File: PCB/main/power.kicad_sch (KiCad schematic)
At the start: 19 parts

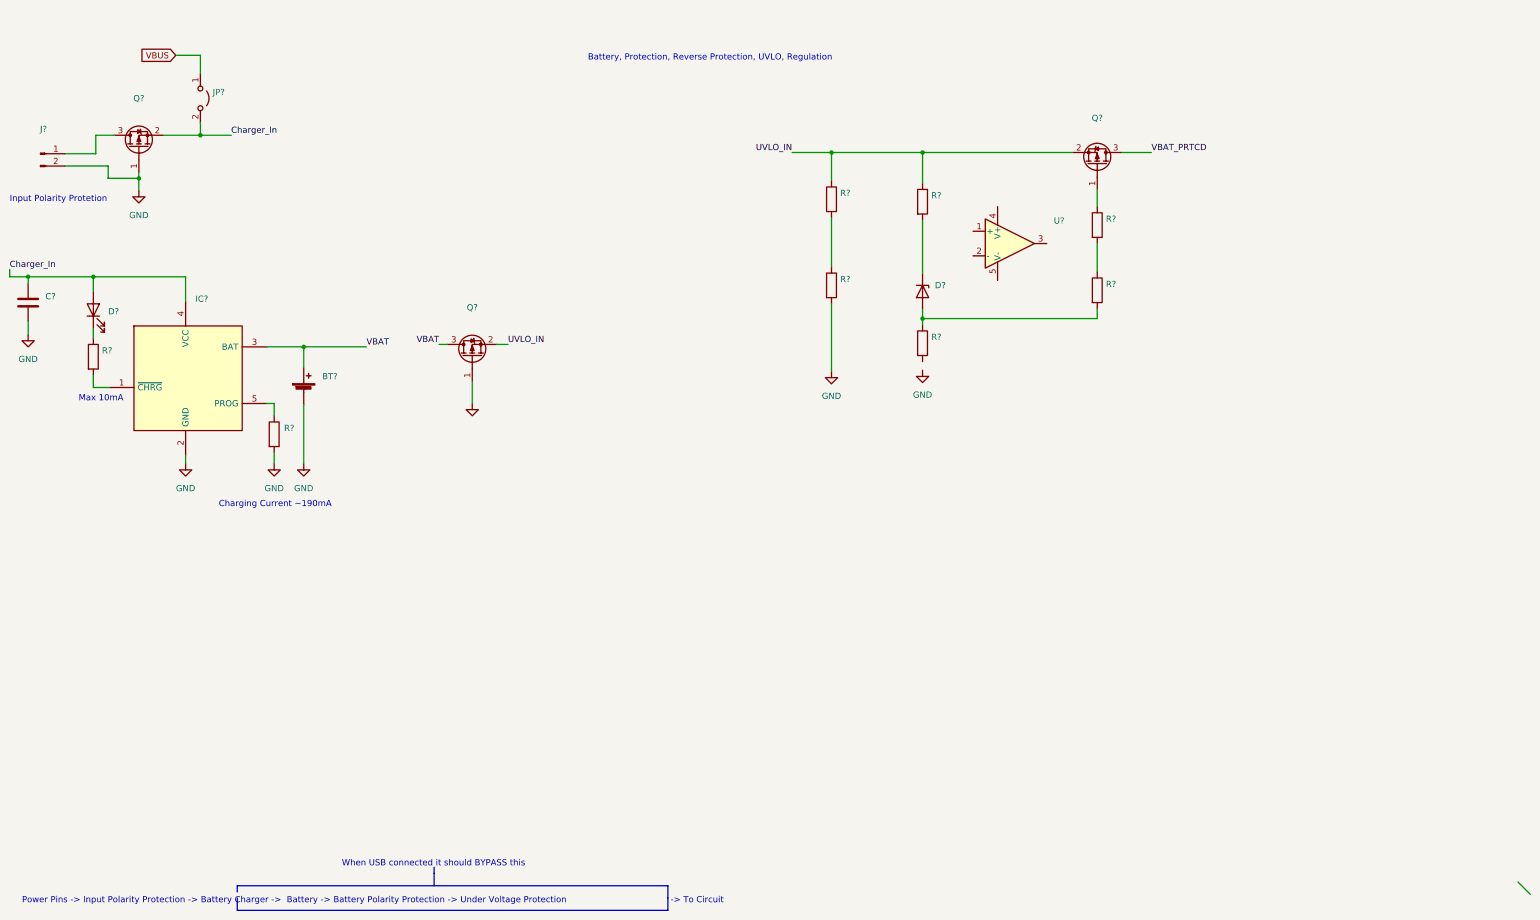
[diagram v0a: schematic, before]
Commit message: updated UVLO circuit
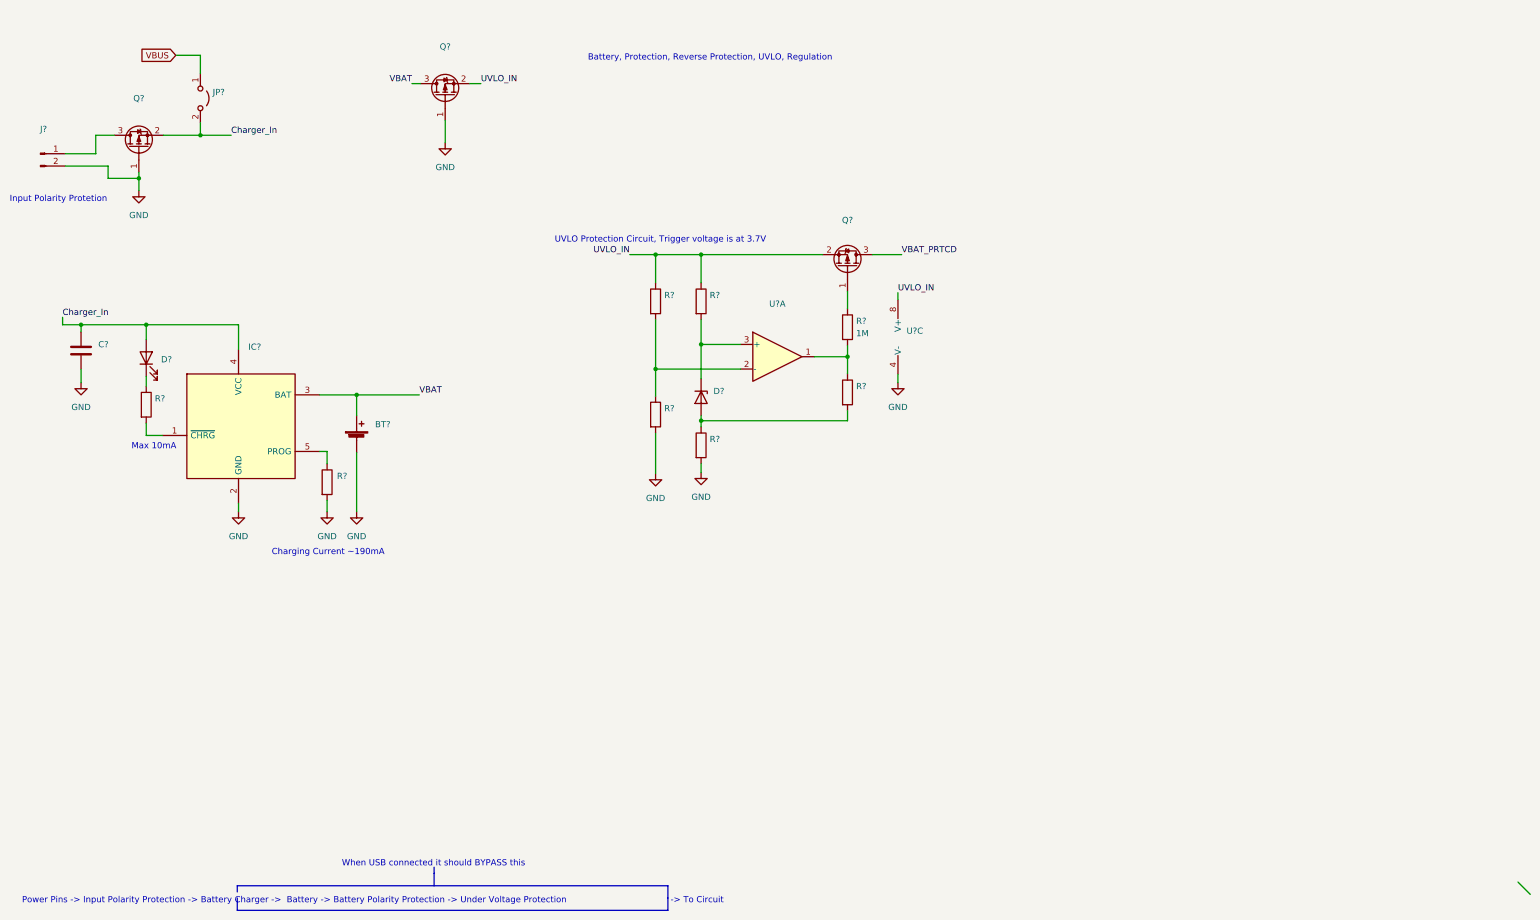
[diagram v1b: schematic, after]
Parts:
- removed R?: (no value), symbol Device:R
- removed U?: (no value), symbol pspice:OPAMP
- added R?: 1M, Resistor_SMD:R_0603_1608Metric_Pad0.98x0.95mm_HandSolder, symbol Device:R
- added U? (x2): (no value), symbol Amplifier_Operational:LM358
- R?: Populate (none) -> Y; Price (none) -> 0.0013
- R?: Populate (none) -> Y; Price (none) -> 0.0014
- R?: LCSC (none) -> C8218; Price (none) -> 0.0013
- R?: LCSC (none) -> C22775; Populate (none) -> Y; Price (none) -> 0.0013
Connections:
- net GND: now also R?.2, U?.4 (V-)
- net UVLO_IN: now also U?.8 (V+)
- net at Q?.1 (G): now also R?.1
- net at R?.1, R?.2: now also U?.2 (-)
- net at D?.1 (K), R?.2: now also U?.3 (+)
- net at R?.1: now also R?.2, U?.1
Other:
- note added: "UVLO Protection Circuit, Trigger voltage is at 3.7V"
- moved on the sheet: BT?, C?, D?, IC?, Q?, R?

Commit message: added digital sensors
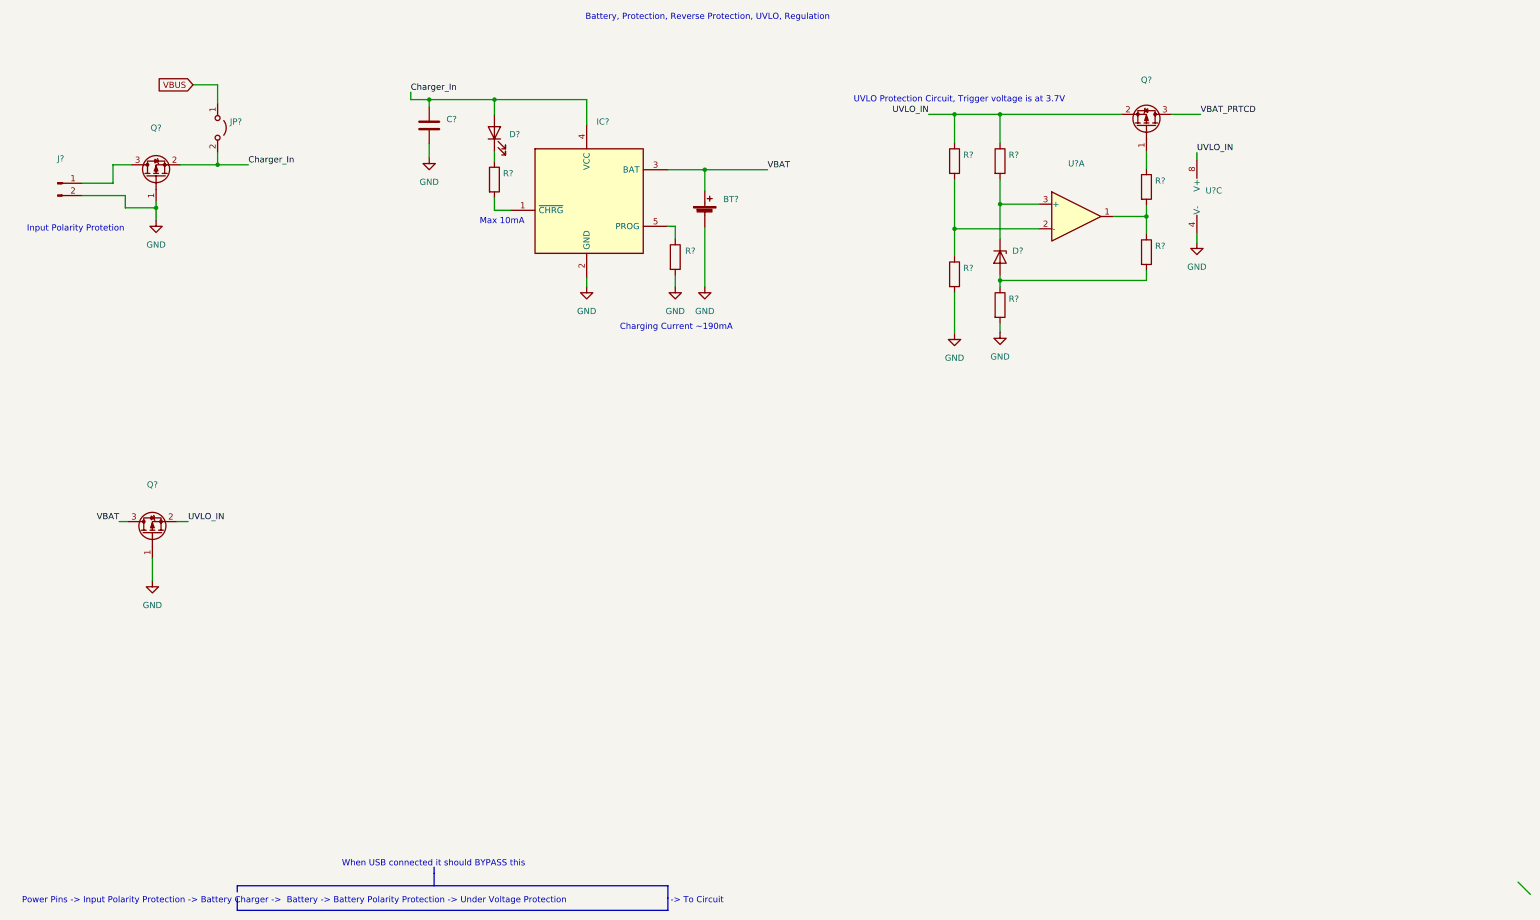
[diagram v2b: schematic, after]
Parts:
- R?: value 1M -> (none); footprint Resistor_SMD:R_0603_1608Metric_Pad0.98x0.95mm_HandSolder -> (none)
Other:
- company: (none) -> University of Cape Town
- title: (none) -> DiscoverAir HAT
- moved on the sheet: BT?, C?, D?, IC?, J?, JP?, Q?, R?, U?A, U?C

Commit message: layout started
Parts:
- removed J?: (no value), symbol Connector:Conn_01x02_Male
- removed JP?: (no value), symbol Jumper:Jumper_2_Open
- added C11, C5, C6, C8, C9: 1uF, Capacitor_SMD:C_0603_1608Metric_Pad1.08x0.95mm_HandSolder, symbol Device:C
- added C7: 10nF, Capacitor_SMD:C_0603_1608Metric_Pad1.08x0.95mm_HandSolder, symbol Device:C
- added D4: D_Schottky, Diode_SMD:D_SMA, symbol Device:D_Schottky
- added J8: Conn_01x02_Male, Connector_PinHeader_2.54mm:PinHeader_1x02_P2.54mm_Vertical, symbol Connector:Conn_01x02_Male
- added JP1, JP2: Jumper_3_Open, Connector_PinHeader_2.54mm:PinHeader_1x03_P2.54mm_Vertical, symbol Jumper:Jumper_3_Open
- added Q3: Q_PMOS_GSD, Package_TO_SOT_SMD:SOT-23, symbol Device:Q_PMOS_GSD
- added R10: 4k7, Resistor_SMD:R_0603_1608Metric_Pad0.98x0.95mm_HandSolder, symbol Device:R
- added R12: 2.2M, Resistor_SMD:R_0603_1608Metric_Pad0.98x0.95mm_HandSolder, symbol Device:R
- added R13: 1M, Resistor_SMD:R_0603_1608Metric_Pad0.98x0.95mm_HandSolder, symbol Device:R
- added TP2: 1V8, symbol Connector:TestPoint_Alt
- added TP4: UVLO_Out, symbol Connector:TestPoint_Alt
- added TP5: REG_IN, symbol Connector:TestPoint_Alt
- added TP6: VBAT, symbol Connector:TestPoint_Alt
- added TP7: UVLO V+, symbol Connector:TestPoint_Alt
- added TP8: UVLO V-, symbol Connector:TestPoint_Alt
- added U2: SGM2007-3.3XN5/TR, Package_TO_SOT_SMD:SOT-23-5, symbol DiscoverAir:SGM2007-3.3XN5/TR
- added U3: AMS1117-1.8, Package_TO_SOT_SMD:SOT-223-3_TabPin2, symbol Regulator_Linear:AMS1117-1.8
- added unit 2 of U4
- BT1: renamed from BT?; value (none) -> Battery_Cell
- C10: renamed from C?; value (none) -> 1uF; footprint (none) -> Capacitor_SMD:C_0603_1608Metric_Pad1.08x0.95mm_HandSolder; LCSC (none) -> C15849
- D3: renamed from D?; value (none) -> CHRG; footprint (none) -> LED_SMD:LED_0603_1608Metric_Pad1.05x0.95mm_HandSolder; LCSC (none) -> C2286
- D5: renamed from D?; value (none) -> D_Zener; footprint (none) -> Diode_SMD:D_SOD-523
- IC3: renamed from IC?; value (none) -> TP4054-42-SOT25-R; footprint (none) -> TP4054-42-SOT25-R:SOT95P280X100-5N; Manufacturer_Name (none) -> TOP POWER
- Q2, Q4, Q5: renamed from Q?; value (none) -> Q_PMOS_GSD; footprint (none) -> Package_TO_SOT_SMD:SOT-23
- R11: renamed from R?; value (none) -> 5K1; footprint (none) -> Resistor_SMD:R_0805_2012Metric_Pad1.20x1.40mm_HandSolder; LCSC (none) -> C23186
- R14: renamed from R?; value (none) -> 300K; footprint (none) -> Resistor_SMD:R_0603_1608Metric_Pad0.98x0.95mm_HandSolder; LCSC C23146 -> C23024; Price 0.0014 -> 0.0013
- R15, R18: renamed from R?; value (none) -> 1M; footprint (none) -> Resistor_SMD:R_0603_1608Metric_Pad0.98x0.95mm_HandSolder
- R16: renamed from R?; value (none) -> 150; footprint (none) -> Resistor_SMD:R_0603_1608Metric_Pad0.98x0.95mm_HandSolder; LCSC C8218 -> C22808; Price 0.0013 -> 0.0016
- R17: renamed from R?; value (none) -> 100; footprint (none) -> Resistor_SMD:R_0603_1608Metric_Pad0.98x0.95mm_HandSolder
- R19: renamed from R?; value (none) -> R; footprint (none) -> Resistor_SMD:R_0603_1608Metric_Pad0.98x0.95mm_HandSolder
- R9: renamed from R?; value (none) -> 510; footprint (none) -> Resistor_SMD:R_0603_1608Metric_Pad0.98x0.95mm_HandSolder; LCSC (none) -> C23193
- U4: renamed from U?; value (none) -> LM358; footprint (none) -> Package_SO:SOIC-8_3.9x4.9mm_P1.27mm; LCSC (none) -> C7950
- U4: renamed from U?; value (none) -> LM358; footprint (none) -> Package_SO:SOIC-8_3.9x4.9mm_P1.27mm
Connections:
- net Charger_In: now also D4.2 (A), J8.1 (Pin_1), Q3.1 (G), R10.2; no longer C10.1, D3.2 (A), IC3.4 (VCC)
- net GND: now also C11.2, C5.2, C6.2, C7.1, C8.2, C9.2, R10.1, R13.2, U2.2 (GND), U3.1 (GND)
- net UVLO_IN: now also R12.1
- net VBAT: now also TP6.1
- net VBAT_PRTCD: now also Q3.3 (D), TP4.1
- net at R14.2, R15.1, U4.2 (-): now also TP7.1
- net at D5.1 (K), R16.2, U4.3 (+): now also TP8.1
- net +5V: now reaches Q2.3 (D)
- net +5V: now also JP1.1 (A), JP2.1 (A)
- new net: C6.1, JP2.2 (C), U3.3 (VI)
- new net: C11.1, R12.2, R13.1, U4.5 (+)
- new net: C10.1, D3.2 (A), IC3.4 (VCC), J8.2 (Pin_2)
- new net: C5.1, JP1.2 (C), U2.1 (IN), U2.3 (EN)
- new net: C7.2, U2.4 (BP)
- new net +1V8: C8.1, TP2.1, U3.2 (VO)
- new net +3V0: C9.1, U2.5 (OUT)
- new net BATTERY_VOLTAGE: U4.6 (-), U4.7
- new net REG_IN: D4.1 (K), JP1.3 (B), JP2.3 (B), Q3.2 (S), TP5.1
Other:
- note added: "1.8V Regulator"
- note added: "3.3V Regulator"
- note added: "Battery Level Sensor"
- note added: "ByPass Battery Switch when USB Powered Allows for battery to charge while circuit is powered by USB"
- note added: "UVLO Protection Circuit, Trigger voltage is at 3.5V"
- note removed: "UVLO Protection Circuit, Trigger voltage is at 3.7V"
- moved on the sheet: Q4

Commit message: started on routing
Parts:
- BT1: footprint (none) -> Battery:BatteryHolder_Keystone_1042_1x18650
- TP2, TP4, TP5, TP6, TP7, TP8: footprint (none) -> TestPoint:TestPoint_Pad_D2.0mm
- U3: value AMS1117-1.8 -> (none); footprint Package_TO_SOT_SMD:SOT-223-3_TabPin2 -> (none)
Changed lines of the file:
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@@
       (effects (font (size 1.27 1.27)) (justify left))
     )
-    (property "Footprint" "" (id 2) (at 132.588 133.096 0)
+    (property "Footprint" "TestPoint:TestPoint_Pad_D2.0mm" (id 2) (at 132.588 133.096 0)
       (effects (font (size 1.27 1.27)) hide)
     )
@@
       (effects (font (size 1.27 1.27)) (justify left))
     )
-    (property "Footprint" "" (id 2) (at 174.244 38.862 0)
+    (property "Footprint" "TestPoint:TestPoint_Pad_D2.0mm" (id 2) (at 174.244 38.862 0)
       (effects (font (size 1.27 1.27)) hide)
     )
@@
     (in_bom yes) (on_board yes) (fields_autoplaced)
     (property "Reference" "U3" (id 0) (at 64.77 134.62 0))
-    (property "Value" "AMS1117-1.8" (id 1) (at 64.77 137.16 0))
-    (property "Footprint" "Package_TO_SOT_SMD:SOT-223-3_TabPin2" (id 2) (at 64.77 136.398 0)
+    (property "Value" "" (id 1) (at 64.77 137.16 0))
+    (property "Footprint" "" (id 2) (at 64.77 136.398 0)
       (effects (font (size 1.27 1.27)) hide)
     )
@@
     (property "Reference" "TP7" (id 0) (at 206.756 43.18 90))
     (property "Value" "UVLO V+" (id 1) (at 208.534 45.974 90))
-    (property "Footprint" "" (id 2) (at 212.852 38.1 0)
+    (property "Footprint" "TestPoint:TestPoint_Pad_D2.0mm" (id 2) (at 212.852 38.1 0)
       (effects (font (size 1.27 1.27)) hide)
     )
@@
       (effects (font (size 1.27 1.27)) (justify left))
     )
-    (property "Footprint" "" (id 2) (at 159.004 133.096 0)
+    (property "Footprint" "TestPoint:TestPoint_Pad_D2.0mm" (id 2) (at 159.004 133.096 0)
       (effects (font (size 1.27 1.27)) hide)
     )
@@
       (effects (font (size 1.27 1.27)) (justify right))
     )
-    (property "Footprint" "" (id 2) (at 77.978 141.478 0)
+    (property "Footprint" "TestPoint:TestPoint_Pad_D2.0mm" (id 2) (at 77.978 141.478 0)
       (effects (font (size 1.27 1.27)) hide)
     )
@@
     (property "Reference" "TP8" (id 0) (at 219.456 46.736 90))
     (property "Value" "UVLO V-" (id 1) (at 220.726 49.784 90))
-    (property "Footprint" "" (id 2) (at 222.25 43.18 0)
+    (property "Footprint" "TestPoint:TestPoint_Pad_D2.0mm" (id 2) (at 222.25 43.18 0)
       (effects (font (size 1.27 1.27)) hide)
     )
@@
       (effects (font (size 1.27 1.27)) (justify left))
     )
-    (property "Footprint" "" (id 2) (at 161.29 46.736 90)
-      (effects (font (size 1.27 1.27)) hide)
-    )
+    (property "Footprint" "Battery:BatteryHolder_Keystone_1042_1x18650" (id 2) (at 161.29 46.736 90)
+      (effects (font (size 1.27 1.27)) hide)
+    )

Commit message: ver 1 complete
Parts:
- added D6: (no value), symbol Device:LED
- added R21: (no value), symbol Device:R
- BT1: value Battery_Cell -> (none); footprint Battery:BatteryHolder_Keystone_1042_1x18650 -> (none)
- C10, C11, C5, C6, C8, C9: value 1uF -> (none); footprint Capacitor_SMD:C_0603_1608Metric_Pad1.08x0.95mm_HandSolder -> (none)
- C7: value 10nF -> (none); footprint Capacitor_SMD:C_0603_1608Metric_Pad1.08x0.95mm_HandSolder -> (none)
- D3: value CHRG -> (none); footprint LED_SMD:LED_0603_1608Metric_Pad1.05x0.95mm_HandSolder -> (none)
- D4: value D_Schottky -> (none); footprint Diode_SMD:D_SMA -> (none)
- D5: value D_Zener -> (none); footprint Diode_SMD:D_SOD-523 -> (none)
- IC3: value TP4054-42-SOT25-R -> (none); footprint TP4054-42-SOT25-R:SOT95P280X100-5N -> (none)
- J8: value Conn_01x02_Male -> (none); footprint Connector_PinHeader_2.54mm:PinHeader_1x02_P2.54mm_Vertical -> (none)
- JP1, JP2: value Jumper_3_Open -> (none); footprint Connector_PinHeader_2.54mm:PinHeader_1x03_P2.54mm_Vertical -> (none)
- Q2, Q3, Q4, Q5: value Q_PMOS_GSD -> (none); footprint Package_TO_SOT_SMD:SOT-23 -> (none)
- R10: value 4k7 -> (none); footprint Resistor_SMD:R_0603_1608Metric_Pad0.98x0.95mm_HandSolder -> (none)
- R11: value 5K1 -> (none); footprint Resistor_SMD:R_0805_2012Metric_Pad1.20x1.40mm_HandSolder -> (none)
- R12: value 2.2M -> (none); footprint Resistor_SMD:R_0603_1608Metric_Pad0.98x0.95mm_HandSolder -> (none)
- R13, R15, R18: value 1M -> (none); footprint Resistor_SMD:R_0603_1608Metric_Pad0.98x0.95mm_HandSolder -> (none)
- R14: value 300K -> (none); footprint Resistor_SMD:R_0603_1608Metric_Pad0.98x0.95mm_HandSolder -> (none)
- R16: value 150 -> (none); footprint Resistor_SMD:R_0603_1608Metric_Pad0.98x0.95mm_HandSolder -> (none)
- R17: value 100 -> (none); footprint Resistor_SMD:R_0603_1608Metric_Pad0.98x0.95mm_HandSolder -> (none)
- R19: value R -> (none); footprint Resistor_SMD:R_0603_1608Metric_Pad0.98x0.95mm_HandSolder -> (none); LCSC (none) -> C22938
- R9: value 510 -> (none); footprint Resistor_SMD:R_0603_1608Metric_Pad0.98x0.95mm_HandSolder -> (none)
- TP2: value 1V8 -> (none); footprint TestPoint:TestPoint_Pad_D2.0mm -> (none)
- TP4: value UVLO_Out -> (none); footprint TestPoint:TestPoint_Pad_D2.0mm -> (none)
- TP5: value REG_IN -> (none); footprint TestPoint:TestPoint_Pad_D2.0mm -> (none)
- TP6: value VBAT -> (none); footprint TestPoint:TestPoint_Pad_D2.0mm -> (none)
- TP7: value UVLO V+ -> (none); footprint TestPoint:TestPoint_Pad_D2.0mm -> (none)
- TP8: value UVLO V- -> (none); footprint TestPoint:TestPoint_Pad_D2.0mm -> (none)
- U2: value SGM2007-3.3XN5/TR -> (none); footprint Package_TO_SOT_SMD:SOT-23-5 -> (none)
- U4: value LM358 -> (none); footprint Package_SO:SOIC-8_3.9x4.9mm_P1.27mm -> (none)
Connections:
- net +3V0: now also D6.2 (A)
- net GND: now also R21.2
- new net: D6.1 (K), R21.1
